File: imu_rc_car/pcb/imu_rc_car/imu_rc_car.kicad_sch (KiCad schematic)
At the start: 32 parts, among them J1 LiPo Battery, J2 Left Terminal, J3 Right Terminal, J4 Prox Sensor FS, J5 Prox Sensor LS, J6 Prox Sensor RS, J7 Prox Sensor BS, J8 Encoder F, J9 Encoder B, Q1 IRLML6344TRPBF, Q2 DMP3160L-7, Q3 IRLZ34N, SW1 SW_Nidec_CAS-120A1, U1 ESP32-S3-DevKitC, U3 AMS1117-3.3, U6 DRV8833PWP, U7 DRV8833PWP

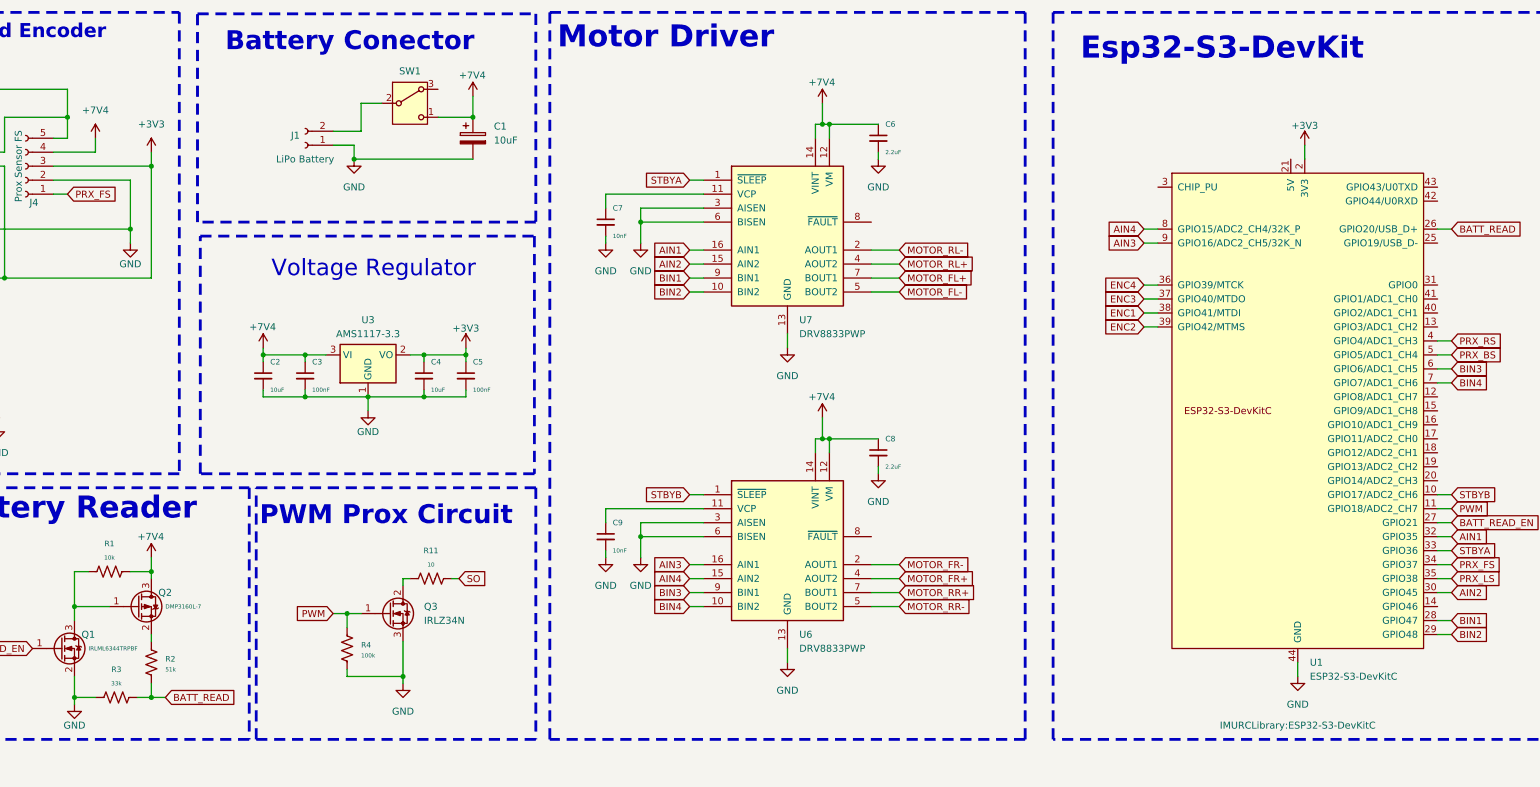
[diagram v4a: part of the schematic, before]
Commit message: commit #32
costs table 4
first revision of imu rc car pcb
imu rc encoders final version v1.0.0 (ordered)
imu rc prox sensors final version v1.0.0 (ordered)
minor resistors tolerance changes in hand unit
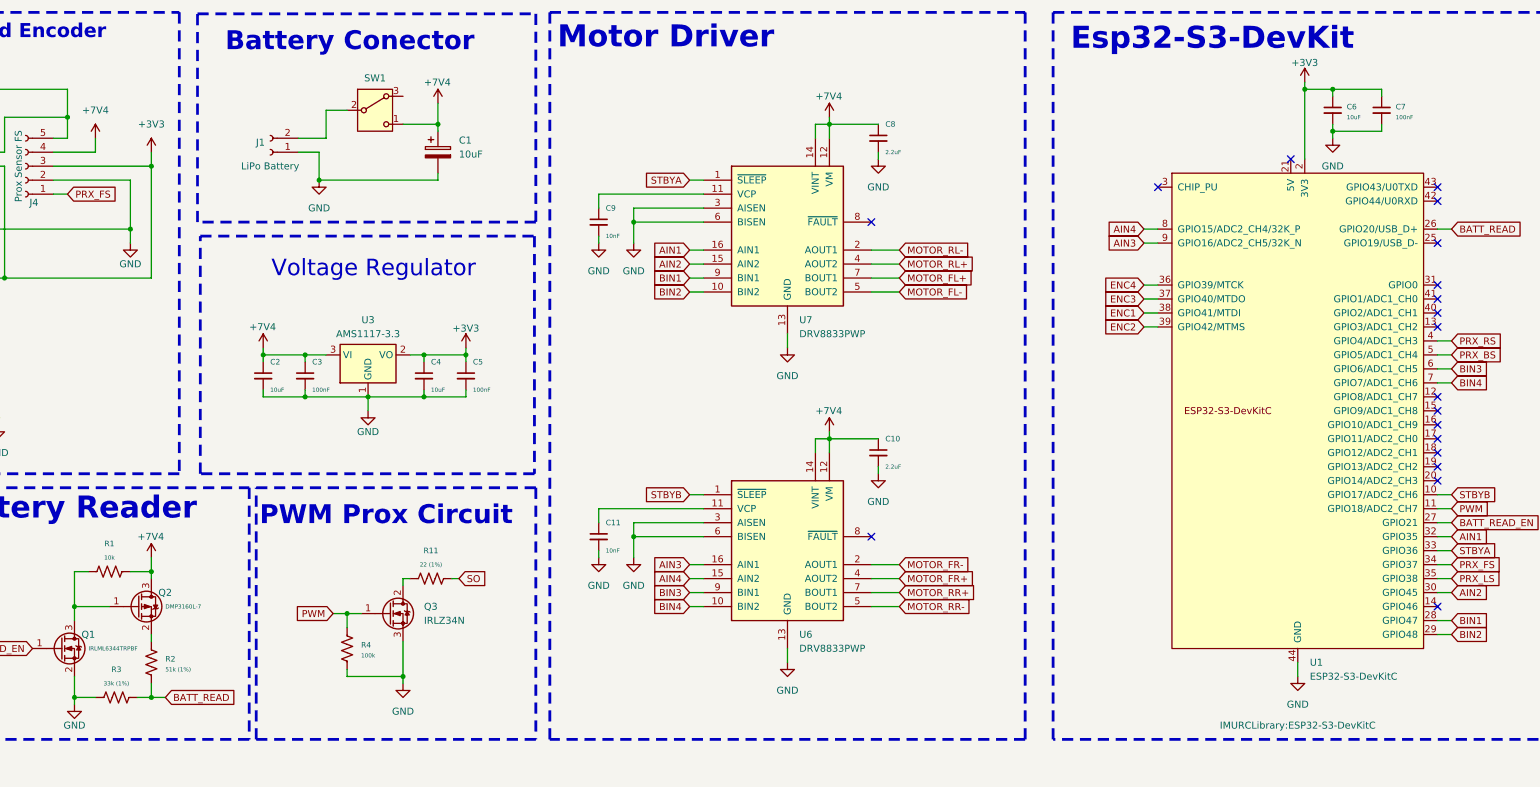
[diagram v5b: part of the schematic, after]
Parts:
- added C6: 10uF, Capacitor_SMD:C_0805_2012Metric, symbol Device:C_Small
- added C7: 100nF, Capacitor_SMD:C_0805_2012Metric, symbol Device:C_Small
- R11: value 10 -> 22 (1%)
- R2: value 51k -> 51k (1%)
- R3: value 33k -> 33k (1%)
- renumbered C8 to C10, C9 to C11, C6 to C8, C7 to C9
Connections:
- net +3V3: now also C6.1, C7.1
- net GND: now also C6.2, C7.2
- no-connect marks 0 -> 19
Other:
- moved on the sheet: C1, C11, C9, J1, SW1

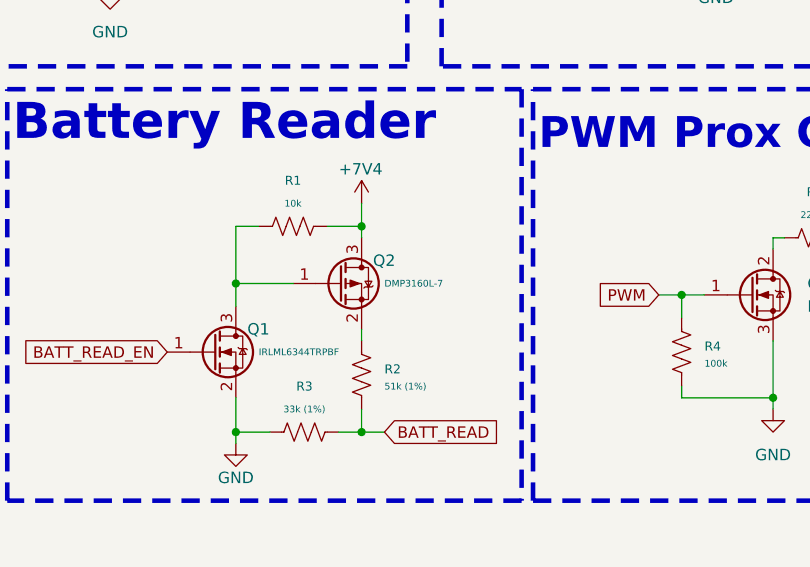
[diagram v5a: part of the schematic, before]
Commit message: commit #34
pcb hand unit v1.1.0:
chaged RGB led footprint to better fit
switch drain with source in Q5 MOSFET (battery reader)

pcb car v1.1.0:
removed power planes, added traces only
switch drain with source in Q1 MOSFET (battery reader)
changed LDO position

code:
changed esp32 devkit to esp32s3 devkit
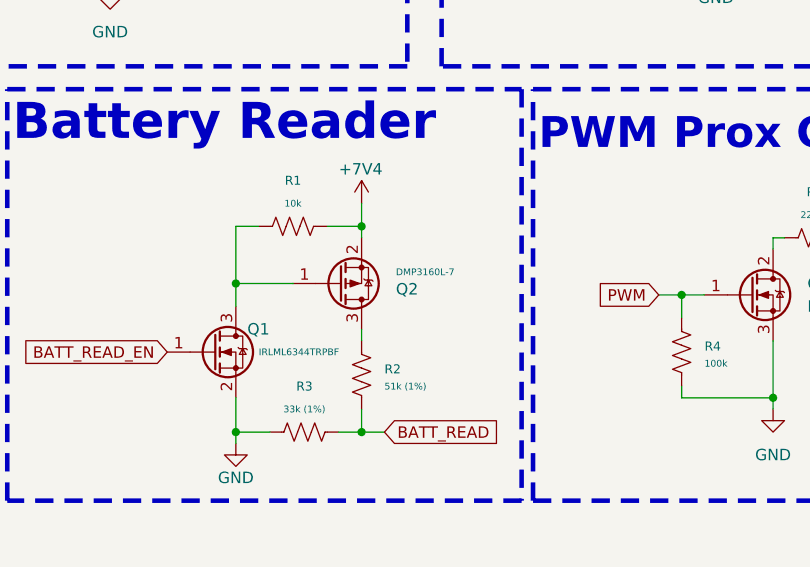
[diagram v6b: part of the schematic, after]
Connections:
- net +7V4: now also Q2.2 (S); no longer Q2.3 (D)
- net at R2.1: now also Q2.3 (D); no longer Q2.2 (S)
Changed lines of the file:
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@@
 	(wire
 		(pts
-			(xy 116.84 128.27) (xy 116.84 129.54)
-		)
-		(stroke
-			(width 0)
-			(type default)
-		)
-	)
-	(wire
-		(pts
 			(xy 237.49 38.1) (xy 237.49 35.56)
 		)
@@
 	(wire
 		(pts
+			(xy 116.84 128.27) (xy 116.84 129.54)
+		)
+		(stroke
+			(width 0)
+			(type default)
+		)
+	)
+	(wire
+		(pts
 			(xy 331.47 35.56) (xy 331.47 36.83)
 		)
@@
 		(lib_id "Transistor_FET:AO3401A")
 		(at 114.3 123.19 0)
+		(mirror x)
 		(unit 1)
 		(exclude_from_sim no)
@@
 		(dnp no)
 		(property "Reference" "Q2"
-			(at 118.11 120.65 0)
+			(at 120.65 123.8251 0)
 			(effects
 				(font
@@
 		)
 		(property "Value" "DMP3160L-7"
-			(at 119.38 123.19 0)
+			(at 120.65 121.9201 0)
 			(effects
 				(font
@@
 		)
 		(property "Footprint" "Package_TO_SOT_SMD:SOT-23"
-			(at 119.38 125.095 0)
+			(at 119.38 121.285 0)
 			(effects
 				(font
@@
 		)
 		(property "Datasheet" "http://www.aosmd.com/pdfs/datasheet/AO3401A.pdf"
-			(at 119.38 127 0)
+			(at 119.38 119.38 0)
 			(effects
 				(font

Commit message: commit #35
fixed error in pcb for DRV8833
added 4 motor support for code
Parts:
- added C12: 2u2F, Capacitor_SMD:C_0805_2012Metric, symbol Device:C_Small
- added C13: 10uF, Capacitor_SMD:C_0805_2012Metric, symbol Device:C_Small
- C10: value 2.2uF -> 10uF
- C8: value 2.2uF -> 10nF
- C9: value 10nF -> 2u2F
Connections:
- net +7V4: now also C11.1, C13.1; no longer U6.14 (VINT), U7.14 (VINT)
- net GND: now also C9.1, C12.1, C13.2; no longer C11.2, C8.2, C9.2
- net at U7.11 (VCP): now also C8.2; no longer C9.1
- net at U6.11 (VCP): now also C11.2; no longer C11.1
- new net: C9.2, U7.14 (VINT)
- new net: C12.2, U6.14 (VINT)

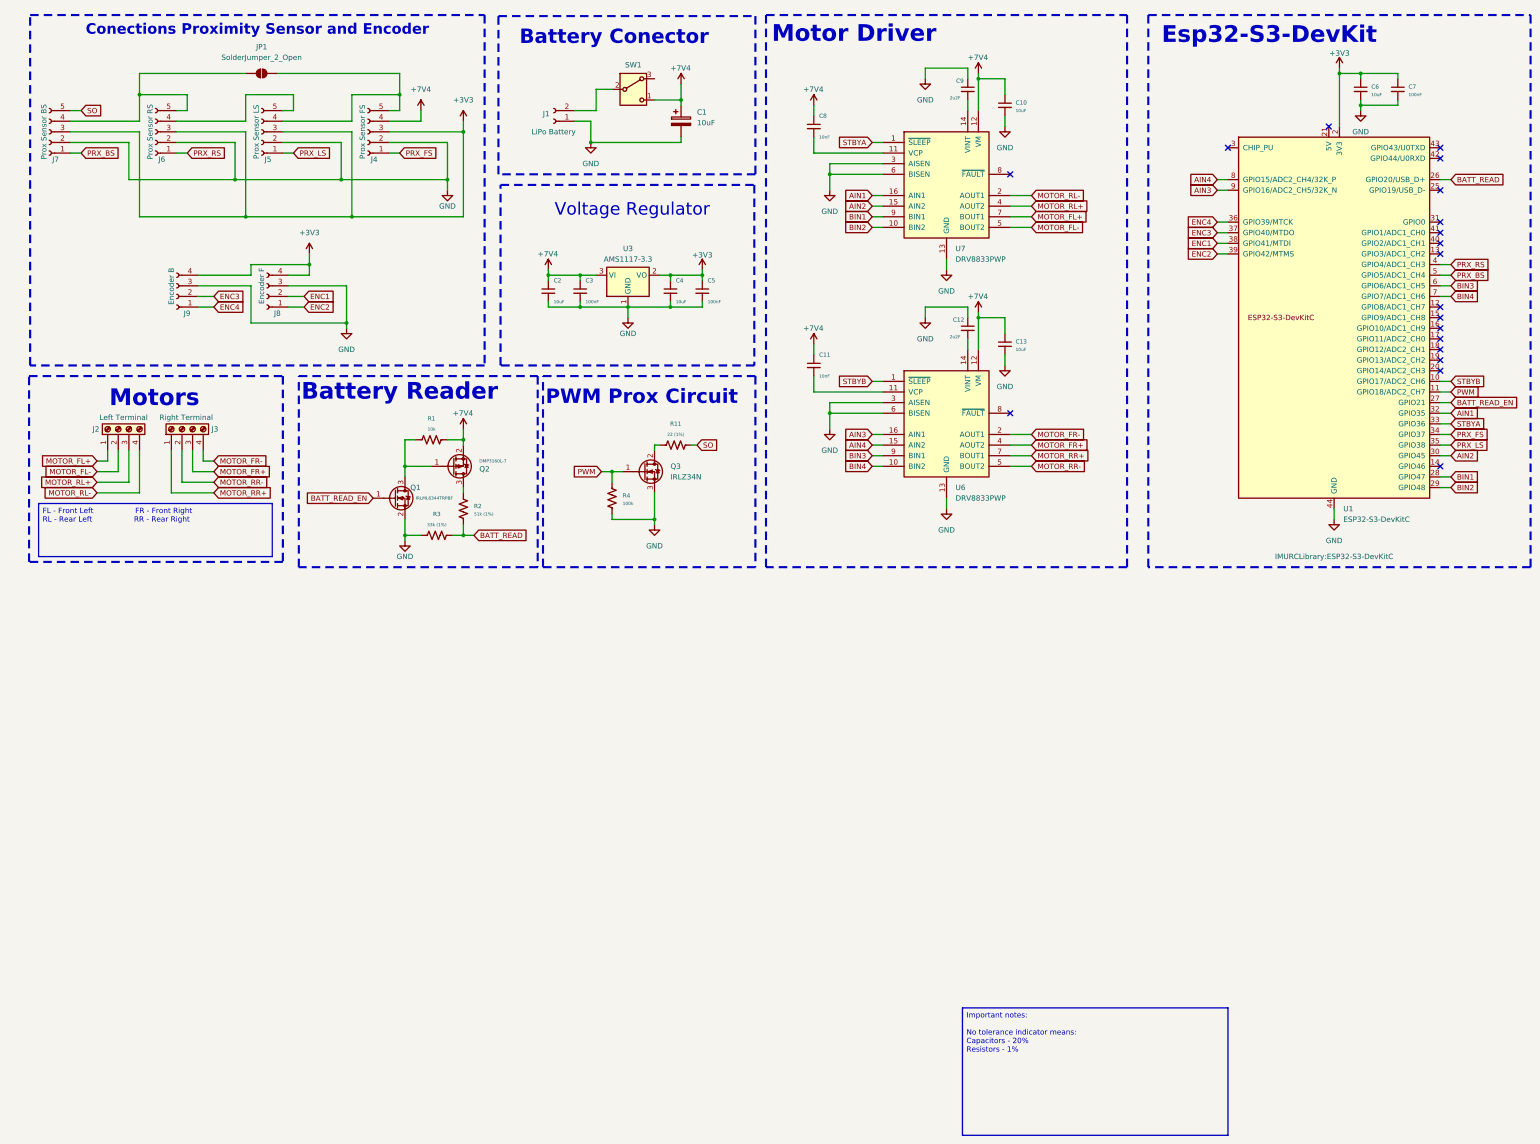
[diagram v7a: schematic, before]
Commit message: commit #38
imu rc car v1.1.1:
Added ON/OFF text for switch
Fixed no ADC GPIOs for 2 prox sensors
Fixed battery reading
Bigger text in Prox Sensors and Encoders
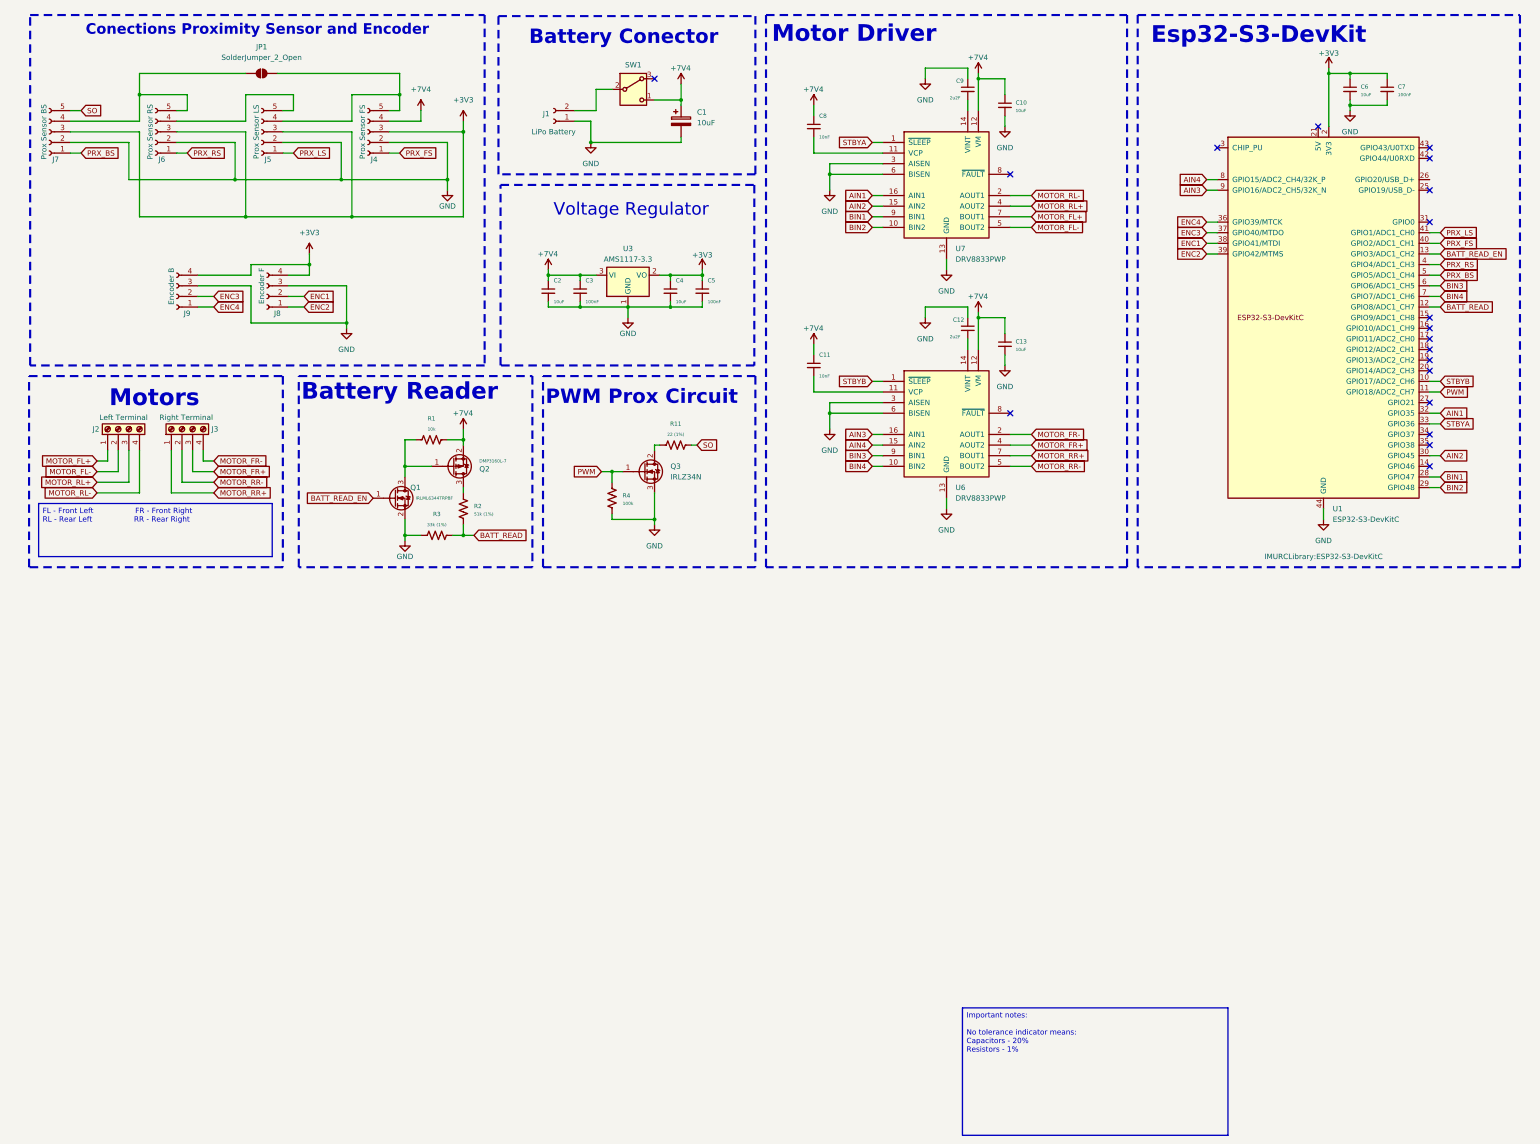
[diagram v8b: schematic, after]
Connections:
- net BATT_READ: now also U1.12 (GPIO8/ADC1_CH7); no longer U1.26 (GPIO20/USB_D+)
- net BATT_READ_EN: now also U1.13 (GPIO3/ADC1_CH2); no longer U1.27 (GPIO21)
- net PRX_FS: now also U1.40 (GPIO2/ADC1_CH1); no longer U1.34 (GPIO37)
- net PRX_LS: now also U1.41 (GPIO1/ADC1_CH0); no longer U1.35 (GPIO38)
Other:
- title: IMU-RC Car -> IMU-RC Car Schematic
- moved on the sheet: C6, C7, U1
